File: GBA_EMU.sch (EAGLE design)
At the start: 99 parts, among them J1 USB-MINIB-5PIN, J2 AVR_SPI, SW1 LEFT, SW2 RIGHT, SW3 PWR_SWITCH, U1 MIC7221, U2 MCP1642B-ADJ, U4 LM4875, U5 Mic5365-2.8Y, U7 AZV321, X2 HEADPHONE

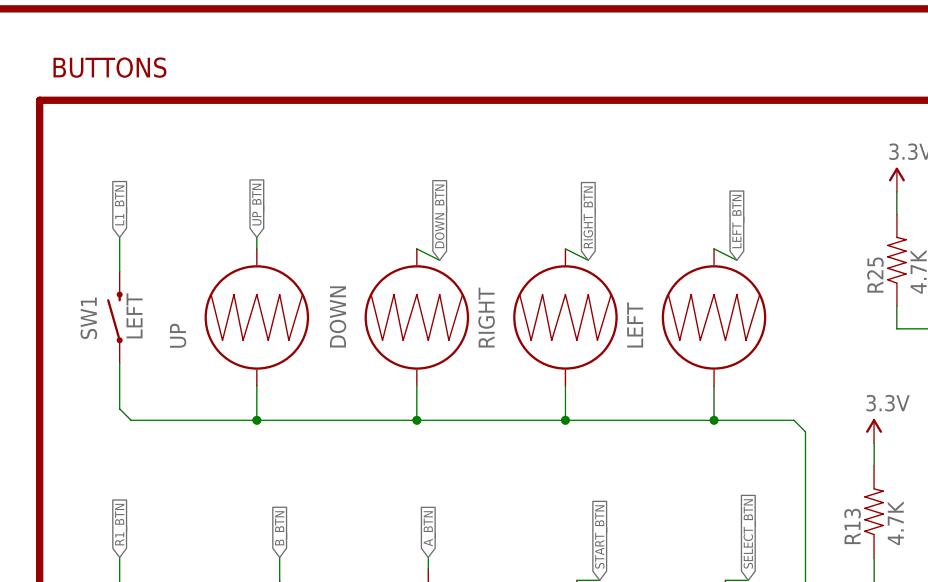
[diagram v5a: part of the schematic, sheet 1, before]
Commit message: added power enable to Coprocessor
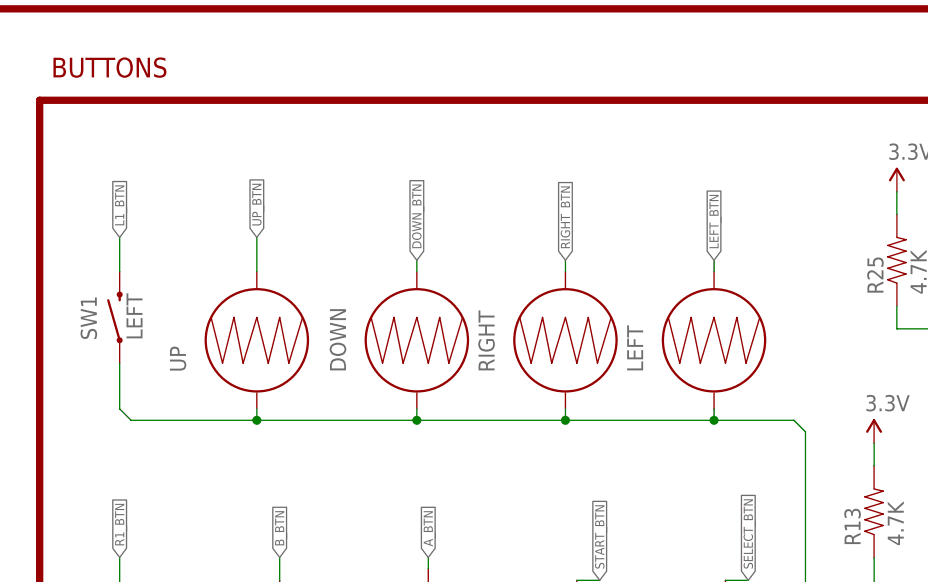
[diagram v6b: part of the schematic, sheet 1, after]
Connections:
- removed net N$38: R24.2
- new net N$44: COPRO.PD0(INT0/OC0B), R24.1
- net GND: now also R23.1
- net PWR_EN: now also R23.2, R24.2; no longer COPRO.PD0(INT0/OC0B), R24.1
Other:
- moved on the sheet: DOWN, LEFT, R23, RIGHT, UP
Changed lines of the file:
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@@
 <part name="SUPPLY38" library="SparkFun-Aesthetics" deviceset="1.8V" device=""/>
 <part name="R24" library="SparkFun-Resistors" deviceset="10KOHM-1/10W-1%(0603)" device="0603" value="10K"/>
+<part name="GND39" library="SparkFun-Aesthetics" deviceset="GND" device=""/>
 </parts>
 <sheets>
@@
 </plain>
 <instances>
-<instance part="UP" gate="S$1" x="332.74" y="26.67" rot="R90"/>
+<instance part="UP" gate="S$1" x="332.74" y="24.13" rot="R90"/>
 <instance part="START" gate="G$1" x="368.3" y="-10.16" rot="R90"/>
 <instance part="R1" gate="R$1" x="335.28" y="170.18"/>
-<instance part="DOWN" gate="S$1" x="350.52" y="26.67" rot="R90"/>
-<instance part="LEFT" gate="S$1" x="383.54" y="26.67" rot="R90"/>
-<instance part="RIGHT" gate="S$1" x="367.03" y="26.67" rot="R90"/>
+<instance part="DOWN" gate="S$1" x="350.52" y="24.13" rot="R90"/>
+<instance part="LEFT" gate="S$1" x="383.54" y="24.13" rot="R90"/>
+<instance part="RIGHT" gate="S$1" x="367.03" y="24.13" rot="R90"/>
 <instance part="SEL" gate="G$1" x="384.81" y="-10.16" rot="R90"/>
 <instance part="A" gate="S$1" x="351.79" y="-8.89" rot="R90"/>
@@
 <pinref part="UP" gate="S$1" pin="1"/>
 <wire x1="393.7" y1="-20.32" x2="393.7" y2="13.97" width="0.1524" layer="91"/>
-<wire x1="332.74" y1="19.05" x2="332.74" y2="15.24" width="0.1524" layer="91"/>
+<wire x1="332.74" y1="16.51" x2="332.74" y2="15.24" width="0.1524" layer="91"/>
 <wire x1="332.74" y1="15.24" x2="350.52" y2="15.24" width="0.1524" layer="91"/>
 <pinref part="LEFT" gate="S$1" pin="1"/>
@@
 <wire x1="367.03" y1="15.24" x2="383.54" y2="15.24" width="0.1524" layer="91"/>
 <wire x1="383.54" y1="15.24" x2="392.43" y2="15.24" width="0.1524" layer="91"/>
-<wire x1="383.54" y1="19.05" x2="383.54" y2="15.24" width="0.1524" layer="91"/>
+<wire x1="383.54" y1="16.51" x2="383.54" y2="15.24" width="0.1524" layer="91"/>
 <pinref part="RIGHT" gate="S$1" pin="1"/>
-<wire x1="367.03" y1="19.05" x2="367.03" y2="15.24" width="0.1524" layer="91"/>
+<wire x1="367.03" y1="16.51" x2="367.03" y2="15.24" width="0.1524" layer="91"/>
 <pinref part="DOWN" gate="S$1" pin="1"/>
-<wire x1="350.52" y1="19.05" x2="350.52" y2="15.24" width="0.1524" layer="91"/>
+<wire x1="350.52" y1="16.51" x2="350.52" y2="15.24" width="0.1524" layer="91"/>
 <pinref part="SW1" gate="SW$1" pin="1"/>
 <wire x1="317.5" y1="21.59" x2="317.5" y2="16.51" width="0.1524" layer="91"/>
@@
 <segment>
 <pinref part="UP" gate="S$1" pin="2"/>
-<wire x1="332.74" y1="34.29" x2="332.74" y2="35.56" width="0.1524" layer="91"/>
+<wire x1="332.74" y1="31.75" x2="332.74" y2="35.56" width="0.1524" layer="91"/>
 <label x="332.74" y="35.56" size="1.016" layer="95" rot="R90" xref="yes"/>
 </segment>
@@
 <segment>
 <pinref part="DOWN" gate="S$1" pin="2"/>
-<wire x1="350.52" y1="34.29" x2="353.06" y2="33.02" width="0.1524" layer="91"/>
-<label x="353.06" y="33.02" size="1.016" layer="95" rot="R90" xref="yes"/>
+<wire x1="350.52" y1="31.75" x2="350.52" y2="33.02" width="0.1524" layer="91"/>
+<label x="350.52" y="33.02" size="1.016" layer="95" rot="R90" xref="yes"/>
 </segment>
 </net>
@@
 <segment>
 <pinref part="RIGHT" gate="S$1" pin="2"/>
-<wire x1="367.03" y1="34.29" x2="369.57" y2="33.02" width="0.1524" layer="91"/>
-<label x="369.57" y="33.02" size="1.016" layer="95" rot="R90" xref="yes"/>
+<wire x1="367.03" y1="31.75" x2="367.03" y2="33.02" width="0.1524" layer="91"/>
+<label x="367.03" y="33.02" size="1.016" layer="95" rot="R90" xref="yes"/>
 </segment>
 </net>
@@
 <segment>
 <pinref part="LEFT" gate="S$1" pin="2"/>
-<wire x1="383.54" y1="34.29" x2="386.08" y2="33.02" width="0.1524" layer="91"/>
-<label x="386.08" y="33.02" size="1.016" layer="95" rot="R90" xref="yes"/>
+<wire x1="383.54" y1="31.75" x2="383.54" y2="33.02" width="0.1524" layer="91"/>
+<label x="383.54" y="33.02" size="1.016" layer="95" rot="R90" xref="yes"/>
 </segment>
 </net>
@@
 <net name="PWR_EN" class="0">
 <segment>
-<pinref part="COPRO" gate="G$1" pin="PD0(INT0/OC0B)"/>
-<wire x1="104.14" y1="139.7" x2="106.68" y2="139.7" width="0.1524" layer="91"/>
-<wire x1="106.68" y1="139.7" x2="106.68" y2="162.56" width="0.1524" layer="91"/>
-<wire x1="106.68" y1="162.56" x2="114.3" y2="162.56" width="0.1524" layer="91"/>
-<label x="129.54" y="162.56" size="1.778" layer="95" xref="yes"/>
-<pinref part="R24" gate="G$1" pin="1"/>
-</segment>
-</net>
-<net name="N$38" class="0">
-<segment>
 <pinref part="R24" gate="G$1" pin="2"/>
 <wire x1="129.54" y1="162.56" x2="124.46" y2="162.56" width="0.1524" layer="91"/>
+<label x="129.54" y="162.56" size="1.778" layer="95" xref="yes"/>
+</segment>
+</net>
+<net name="N$44" class="0">
+<segment>
+<pinref part="COPRO" gate="G$1" pin="PD0(INT0/OC0B)"/>
+<wire x1="104.14" y1="139.7" x2="109.22" y2="139.7" width="0.1524" layer="91"/>
+<wire x1="109.22" y1="139.7" x2="109.22" y2="162.56" width="0.1524" layer="91"/>
+<pinref part="R24" gate="G$1" pin="1"/>
+<wire x1="109.22" y1="162.56" x2="114.3" y2="162.56" width="0.1524" layer="91"/>
 </segment>
 </net>
@@
 <instance part="SW8" gate="G$1" x="35.56" y="134.62"/>
 <instance part="D2" gate="G$1" x="33.02" y="149.86"/>
-<instance part="R23" gate="G$1" x="25.4" y="99.06" rot="R90"/>
+<instance part="R23" gate="G$1" x="33.02" y="99.06" rot="R90"/>
 <instance part="D3" gate="G$1" x="40.64" y="149.86"/>
 <instance part="D4" gate="G$1" x="48.26" y="149.86"/>
@@
 <instance part="D5" gate="D$1" x="20.32" y="139.7"/>
 <instance part="D6" gate="D$1" x="20.32" y="132.08"/>
+<instance part="GND39" gate="1" x="33.02" y="88.9"/>
 </instances>
 <busses>
@@
 <wire x1="96.52" y1="109.22" x2="96.52" y2="91.44" width="0.1524" layer="91"/>
 <pinref part="GND36" gate="1" pin="GND"/>
+</segment>
+<segment>
+<pinref part="GND39" gate="1" pin="GND"/>
+<pinref part="R23" gate="G$1" pin="1"/>
+<wire x1="33.02" y1="91.44" x2="33.02" y2="93.98" width="0.1524" layer="91"/>
 </segment>
 </net>
@@
 <pinref part="U2" gate="U$1" pin="EN"/>
 <wire x1="45.72" y1="121.92" x2="35.56" y2="121.92" width="0.1524" layer="91"/>
-<wire x1="35.56" y1="121.92" x2="27.94" y2="121.92" width="0.1524" layer="91"/>
 <wire x1="35.56" y1="121.92" x2="35.56" y2="111.76" width="0.1524" layer="91"/>
-<junction x="35.56" y="121.92"/>
-<wire x1="35.56" y1="111.76" x2="30.48" y2="111.76" width="0.1524" layer="91"/>
+<wire x1="35.56" y1="111.76" x2="33.02" y2="111.76" width="0.1524" layer="91"/>
 <label x="30.48" y="111.76" size="1.778" layer="95" rot="R180" xref="yes"/>
-</segment>
-</net>
+<pinref part="R23" gate="G$1" pin="2"/>
+<wire x1="33.02" y1="111.76" x2="30.48" y2="111.76" width="0.1524" layer="91"/>
+<wire x1="33.02" y1="104.14" x2="33.02" y2="111.76" width="0.1524" layer="91"/>
+<junction x="33.02" y="111.76"/>
+</segment>
+</net>

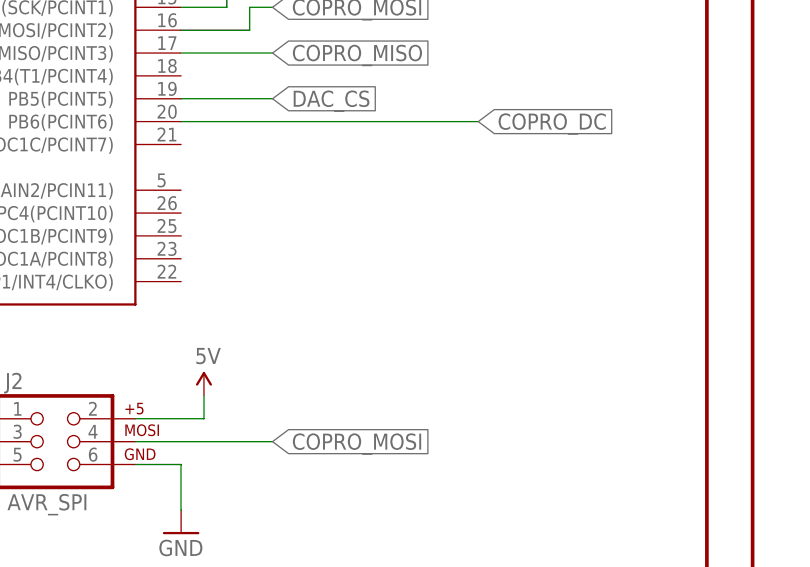
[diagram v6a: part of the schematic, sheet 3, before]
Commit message: added power down
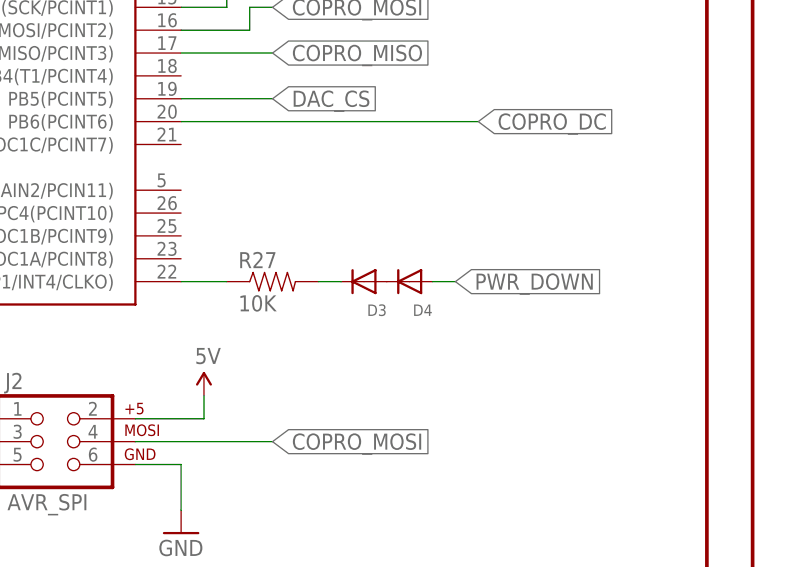
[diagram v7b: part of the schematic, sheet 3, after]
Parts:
- added R27: 10K, SparkFun-Resistors:10KOHM-1/10W-1%(0603)0603
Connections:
- removed net N$32: C14.+, L1.1, SW8.P$2, U2.VIN
- new net N$38: COPRO.PC7(ICP1/INT4/CLKO), R27.1
- new net PWR_DOWN: C14.+, D4.A, L1.1, SW8.P$2, U2.VIN
- net N$31: now also D4.C; no longer D2.C
- net N$33: now also R27.2; no longer D4.A
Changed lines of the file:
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@@
 <part name="D2" library="adafruit" deviceset="DIODE" device="SOD-523"/>
 <part name="R23" library="SparkFun-Resistors" deviceset="100KOHM-1/10W-1%(0603)" device="" value="100k"/>
-<part name="D3" library="adafruit" deviceset="DIODE" device="SOD-523"/>
-<part name="D4" library="adafruit" deviceset="DIODE" device="SOD-523"/>
 <part name="L1" library="SparkFun-Passives" deviceset="INDUCTOR" device="INDUCTOR_4.7UH" value="4.7uH"/>
 <part name="GND36" library="SparkFun-Aesthetics" deviceset="GND" device=""/>
@@
 <part name="R24" library="SparkFun-Resistors" deviceset="10KOHM-1/10W-1%(0603)" device="0603" value="10K"/>
 <part name="GND39" library="SparkFun-Aesthetics" deviceset="GND" device=""/>
+<part name="D3" library="adafruit" deviceset="DIODE" device="SOD-523"/>
+<part name="D4" library="adafruit" deviceset="DIODE" device="SOD-523"/>
+<part name="R27" library="SparkFun-Resistors" deviceset="10KOHM-1/10W-1%(0603)" device="0603" value="10K"/>
 </parts>
 <sheets>
@@
 <instance part="SUPPLY38" gate="G$1" x="68.58" y="30.48"/>
 <instance part="R24" gate="G$1" x="119.38" y="162.56"/>
+<instance part="D3" gate="G$1" x="124.46" y="81.28" rot="R180"/>
+<instance part="D4" gate="G$1" x="129.54" y="81.28" rot="R180"/>
+<instance part="R27" gate="G$1" x="114.3" y="81.28"/>
 </instances>
 <busses>
@@
 <pinref part="R24" gate="G$1" pin="1"/>
 <wire x1="109.22" y1="162.56" x2="114.3" y2="162.56" width="0.1524" layer="91"/>
+</segment>
+</net>
+<net name="N$31" class="0">
+<segment>
+<pinref part="D3" gate="G$1" pin="A"/>
+<pinref part="D4" gate="G$1" pin="C"/>
+</segment>
+</net>
+<net name="N$33" class="0">
+<segment>
+<pinref part="D3" gate="G$1" pin="C"/>
+<pinref part="R27" gate="G$1" pin="2"/>
+<wire x1="121.92" y1="81.28" x2="119.38" y2="81.28" width="0.1524" layer="91"/>
+</segment>
+</net>
+<net name="N$38" class="0">
+<segment>
+<pinref part="R27" gate="G$1" pin="1"/>
+<pinref part="COPRO" gate="G$1" pin="PC7(ICP1/INT4/CLKO)"/>
+<wire x1="109.22" y1="81.28" x2="104.14" y2="81.28" width="0.1524" layer="91"/>
+</segment>
+</net>
+<net name="PWR_DOWN" class="0">
+<segment>
+<pinref part="D4" gate="G$1" pin="A"/>
+<wire x1="132.08" y1="81.28" x2="134.62" y2="81.28" width="0.1524" layer="91"/>
+<label x="134.62" y="81.28" size="1.778" layer="95" xref="yes"/>
 </segment>
 </net>
@@
 <instance part="D2" gate="G$1" x="33.02" y="149.86"/>
 <instance part="R23" gate="G$1" x="33.02" y="99.06" rot="R90"/>
-<instance part="D3" gate="G$1" x="40.64" y="149.86"/>
-<instance part="D4" gate="G$1" x="48.26" y="149.86"/>
 <instance part="L1" gate="G$1" x="53.34" y="144.78" rot="R90"/>
 <instance part="GND36" gate="1" x="96.52" y="88.9"/>
@@
 </segment>
 </net>
-<net name="N$32" class="0">
+<net name="PWR_DOWN" class="0">
 <segment>
 <pinref part="U2" gate="U$1" pin="VIN"/>
@@
 <pinref part="C14" gate="G$1" pin="+"/>
 <wire x1="43.18" y1="129.54" x2="40.64" y2="129.54" width="0.1524" layer="91"/>
-<wire x1="40.64" y1="114.3" x2="40.64" y2="129.54" width="0.1524" layer="91"/>
+<wire x1="40.64" y1="114.3" x2="40.64" y2="124.46" width="0.1524" layer="91"/>
 <pinref part="L1" gate="G$1" pin="1"/>
+<wire x1="40.64" y1="124.46" x2="40.64" y2="129.54" width="0.1524" layer="91"/>
 <wire x1="45.72" y1="144.78" x2="43.18" y2="144.78" width="0.1524" layer="91"/>
 <wire x1="43.18" y1="144.78" x2="43.18" y2="129.54" width="0.1524" layer="91"/>
@@
 <wire x1="40.64" y1="134.62" x2="40.64" y2="129.54" width="0.1524" layer="91"/>
 <junction x="40.64" y="129.54"/>
-</segment>
-</net>
-<net name="N$31" class="0">
-<segment>
-<pinref part="D2" gate="G$1" pin="C"/>
-<pinref part="D3" gate="G$1" pin="A"/>
-<wire x1="35.56" y1="149.86" x2="38.1" y2="149.86" width="0.1524" layer="91"/>
-</segment>
-</net>
-<net name="N$33" class="0">
-<segment>
-<pinref part="D3" gate="G$1" pin="C"/>
-<pinref part="D4" gate="G$1" pin="A"/>
-<wire x1="43.18" y1="149.86" x2="45.72" y2="149.86" width="0.1524" layer="91"/>
-</segment>
-</net>
+<wire x1="40.64" y1="124.46" x2="38.1" y2="124.46" width="0.1524" layer="91"/>
+<junction x="40.64" y="124.46"/>
+<label x="38.1" y="124.46" size="1.778" layer="95" rot="R180" xref="yes"/>
+</segment>
+</net>

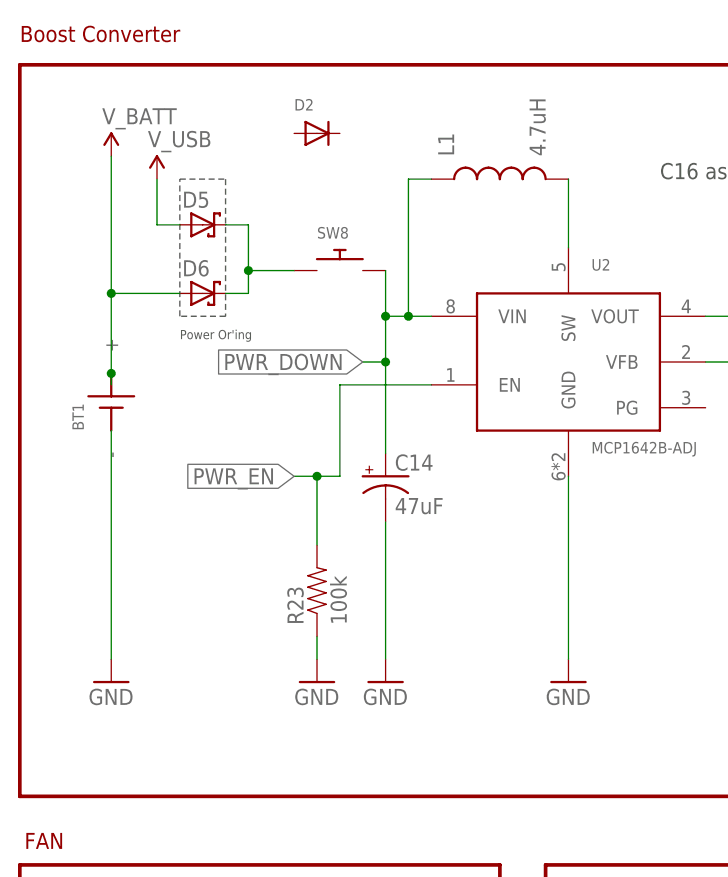
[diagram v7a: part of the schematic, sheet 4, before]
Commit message: correctly wired power up and power down
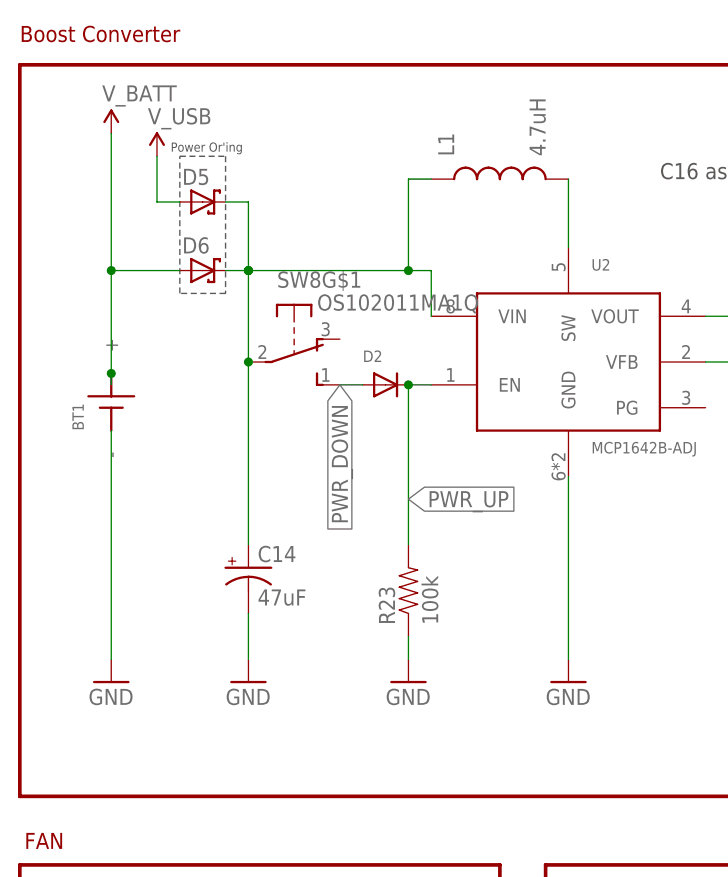
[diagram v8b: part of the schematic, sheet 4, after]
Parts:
- SW8: value (none) -> OS102011MA1Q; device adafruit:SWITCH_PUSHBUTTONSOFTTOUCHSMD_SJ -> adafruit:OS102011MA1Q
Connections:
- removed net N$12: D5.C, D6.C, SW8.P$1
- removed net PWR_EN: R23.2, R24.2, U2.EN
- new net N$45: C14.+, D5.C, D6.C, L1.1, SW8G$1.P, U2.VIN
- new net PWR_UP: D2.C, R23.2, R24.2, U2.EN
- net PWR_DOWN: now also D2.A, SW8G$1.S; no longer C14.+, L1.1, SW8.P$2, U2.VIN
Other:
- moved on the sheet: C14, D2, D5, D6, POT1SW, R23
